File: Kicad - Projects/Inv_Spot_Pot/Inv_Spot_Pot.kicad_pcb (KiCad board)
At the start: 2 copper layers, 190 x 179.5 mm, 107 parts, among them J2 PWM, J3 Display_Power, J4 24V, J5 24V, J6 PWM, K1 Y14x-1C-xxDS, Q1 60N60, Q2 60N60, Q3 60N60, Q4 60N60, U2 LTV-817S

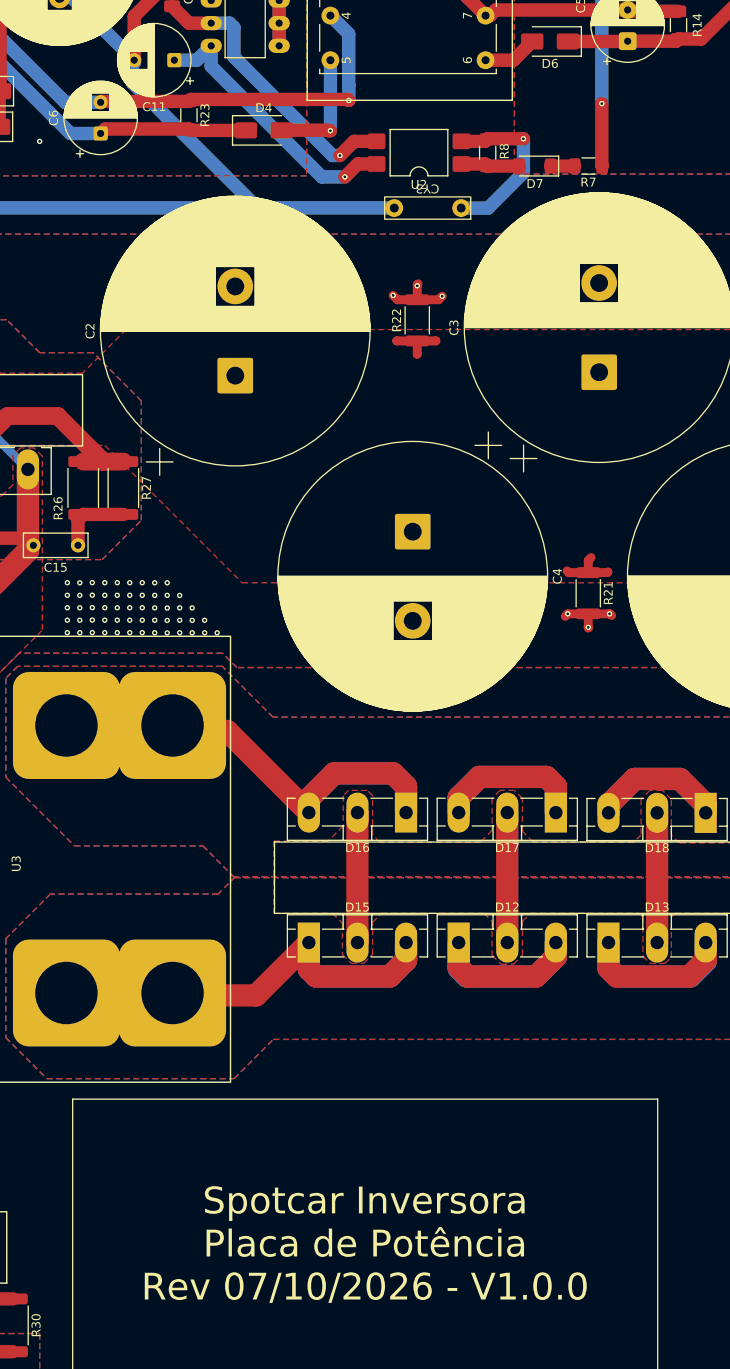
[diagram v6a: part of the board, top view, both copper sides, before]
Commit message: Atualizada Revisão da Placa
Atualizada revisão da placa de potência (07/10/2026, V1.0.0 -> 27/10/2026, V1.1.0)
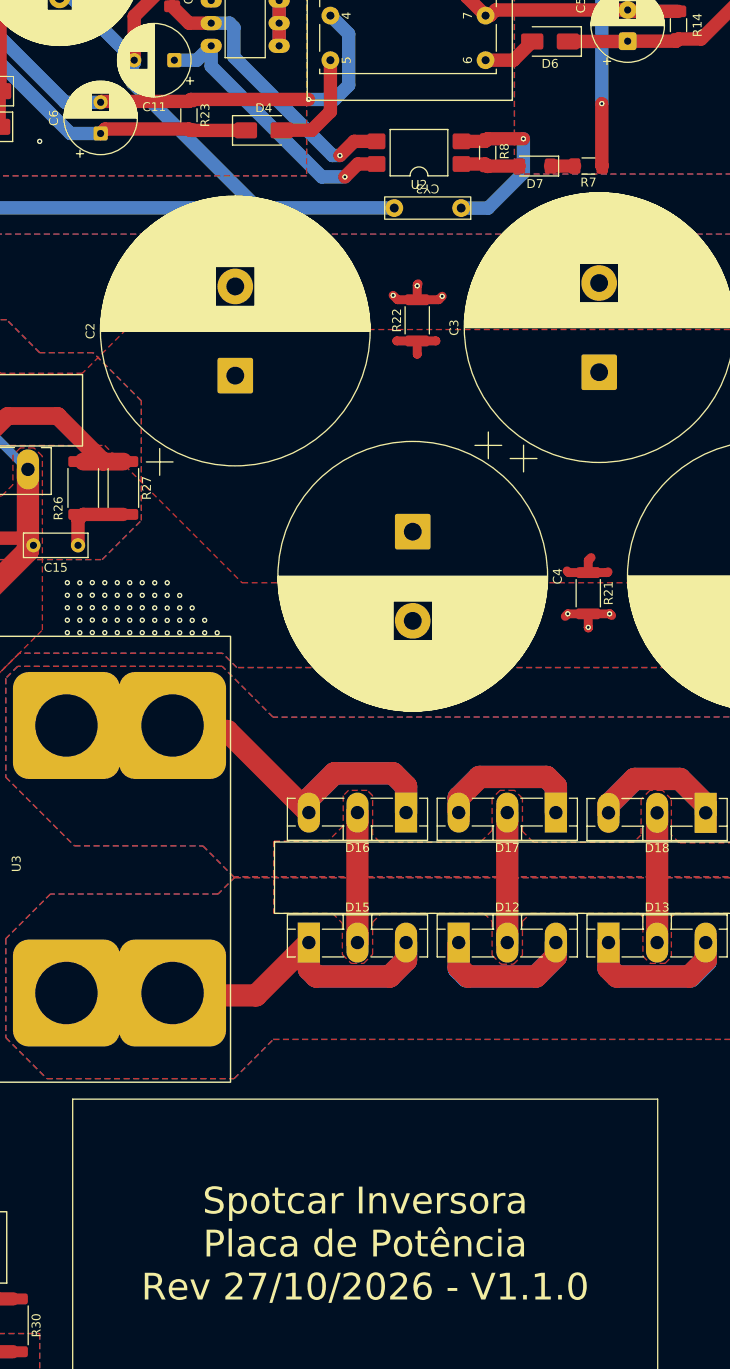
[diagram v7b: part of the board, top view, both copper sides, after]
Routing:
- net Net-(D4-A): track 13.4 -> 12.1 mm, vias 1 -> 0
- net GND_{24}: track 202.5 -> 201.4 mm
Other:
- board text added: "Spotcar Inversora Placa de Potência Rev 27/10/2026 - V1.1.0"
- board text removed: "Spotcar Inversora Placa de Potência Rev 07/10/2026 - V1.0.0"
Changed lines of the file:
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@@
 		(capping no)
 		(filling no)
-		(zone_defaults)
 		(pcbplotparams
 			(layerselection 0x00000000_00000000_55555555_55555571)
@@
 		)
 	)
-	(gr_text "Spotcar Inversora\nPlaca de Potência\nRev 07/10/2026 - V1.0.0"
+	(gr_text "Spotcar Inversora\nPlaca de Potência\nRev 27/10/2026 - V1.1.0"
 		(at 141.9 171.15 0)
 		(layer "F.SilkS")
@@
 	)
 	(segment
-		(start 122.352065 42.8)
-		(end 122.133 43.019065)
-		(width 1.5)
-		(layer "F.Cu")
-		(net "GND_{24}")
-	)
-	(segment
 		(start 17.97 35.3925)
 		(end 17.97 23.68)
@@
 	)
 	(segment
-		(start 139.95 42.8)
-		(end 122.352065 42.8)
-		(width 1.5)
-		(layer "F.Cu")
-		(net "GND_{24}")
-	)
-	(segment
 		(start 22.4525 19.1975)
 		(end 23.83 19.1975)
@@
 	)
 	(segment
+		(start 122.352065 42.8)
+		(end 122.133 43.019065)
+		(width 1.5)
+		(layer "F.Cu")
+		(net "GND_{24}")
+	)
+	(segment
 		(start 82.598 15.909065)
 		(end 81.399497 14.710562)
@@
 	)
 	(segment
+		(start 135.55 42.8)
+		(end 122.352065 42.8)
+		(width 1.5)
+		(layer "F.Cu")
+		(net "GND_{24}")
+	)
+	(segment
 		(start 100.733 15.469065)
 		(end 105.808435 15.469065)
@@
 	)
 	(segment
-		(start 140.06 42.91)
-		(end 139.95 42.8)
-		(width 1.5)
-		(layer "F.Cu")
-		(net "GND_{24}")
-	)
-	(segment
 		(start 81.399497 14.710562)
 		(end 31.879438 14.710562)
@@
 	)
 	(via
-		(at 140.06 42.91)
+		(at 135.55 42.8)
 		(size 0.6)
 		(drill 0.3)
@@
 	)
 	(segment
-		(start 140.06 41.22)
-		(end 140.05 41.21)
+		(start 135.55 42.8)
+		(end 138.46 42.8)
 		(width 1.5)
 		(layer "B.Cu")
@@
 	)
 	(segment
-		(start 140.05 35.45)
-		(end 138 33.4)
+		(start 138.46 42.8)
+		(end 140.05 41.21)
 		(width 1.5)
 		(layer "B.Cu")
@@
 	)
 	(segment
-		(start 140.05 41.21)
-		(end 140.05 35.45)
+		(start 140.05 35.45)
+		(end 138 33.4)
 		(width 1.5)
 		(layer "B.Cu")
@@
 	)
 	(segment
-		(start 140.06 42.91)
-		(end 140.06 41.22)
+		(start 140.05 41.21)
+		(end 140.05 35.45)
 		(width 1.5)
 		(layer "B.Cu")
@@
 	)
 	(segment
-		(start 132.552065 46.25)
-		(end 132.533 46.269065)
+		(start 138 44.17)
+		(end 135.92 46.25)
 		(width 1.5)
 		(layer "F.Cu")
@@
 	)
 	(segment
-		(start 137.72 46.25)
-		(end 132.552065 46.25)
+		(start 132.552065 46.25)
+		(end 132.533 46.269065)
 		(width 1.5)
 		(layer "F.Cu")
@@
 	)
 	(segment
-		(start 138 46.31)
-		(end 137.78 46.31)
+		(start 135.92 46.25)
+		(end 132.552065 46.25)
 		(width 1.5)
 		(layer "F.Cu")
@@
 	)
 	(segment
-		(start 137.78 46.31)
-		(end 137.72 46.25)
+		(start 138 38.4)
+		(end 138 44.17)
 		(width 1.5)
 		(layer "F.Cu")
 		(net "Net-(D4-A)")
 	)
-	(via
-		(at 138 46.31)
-		(size 0.6)
-		(drill 0.3)
-		(layers "F.Cu" "B.Cu")
-		(net "Net-(D4-A)")
-	)
-	(segment
-		(start 138 46.31)
-		(end 138 38.4)
-		(width 1.5)
-		(layer "B.Cu")
-		(net "Net-(D4-A)")
-	)
 	(segment
 		(start 44.033 182.450315)
@@
 	)
 	(segment
+		(start 48.9125 76.76)
+		(end 51.8125 76.76)
+		(width 1.5)
+		(layer "F.Cu")
+		(net "Net-(D8-K)")
+	)
+	(segment
+		(start 51.8125 76.76)
+		(end 52.0025 76.95)
+		(width 1.5)
+		(layer "F.Cu")
+		(net "Net-(D8-K)")
+	)
+	(segment
+		(start 48.521565 73.269065)
+		(end 48.9125 73.66)
+		(width 1.5)
+		(layer "F.Cu")
+		(net "PWM")
+	)
+	(segment
+		(start 51.5825 73.67)
+		(end 48.9225 73.67)
+		(width 1.5)
+		(layer "F.Cu")
+		(net "PWM")
+	)
+	(segment
+		(start 48.9225 73.67)
+		(end 48.9125 73.66)
+		(width 1.5)
+		(layer "F.Cu")
+		(net "PWM")
+	)
+	(segment
+		(start 41.133 73.269065)
+		(end 48.521565 73.269065)
+		(width 1.5)
+		(layer "F.Cu")
+		(net "PWM")
+	)
+	(segment
 		(start 104.083 93.417)
 		(end 104.083 84.284065)
@@
 	)
 	(segment
-		(start 48.521565 73.269065)
-		(end 48.9125 73.66)
-		(width 1.5)
-		(layer "F.Cu")
-		(net "PWM")
-	)
-	(segment
-		(start 51.5825 73.67)
-		(end 48.9225 73.67)
-		(width 1.5)
-		(layer "F.Cu")
-		(net "PWM")
-	)
-	(segment
-		(start 48.9225 73.67)
-		(end 48.9125 73.66)
-		(width 1.5)
-		(layer "F.Cu")
-		(net "PWM")
-	)
-	(segment
-		(start 41.133 73.269065)
-		(end 48.521565 73.269065)
-		(width 1.5)
-		(layer "F.Cu")
-		(net "PWM")
-	)
-	(segment
 		(start 184.5625 24.3)
 		(end 184.5625 19.499565)
@@
 	)
 	(segment
+		(start 93.24 84.341065)
+		(end 93.183 84.284065)
+		(width 1.5)
+		(layer "F.Cu")
+		(net "Gate")
+	)
+	(segment
+		(start 58.62 76.95)
+		(end 56.0025 76.95)
+		(width 1.5)
+		(layer "F.Cu")
+		(net "Gate")
+	)
+	(segment
+		(start 93.24 88.8675)
+		(end 93.24 84.341065)
+		(width 1.5)
+		(layer "F.Cu")
+		(net "Gate")
+	)
+	(segment
+		(start 56.0025 76.95)
+		(end 56.0025 74.99)
+		(width 1.5)
+		(layer "F.Cu")
+		(net "Gate")
+	)
+	(segment
+		(start 56.0025 74.99)
+		(end 54.6825 73.67)
+		(width 1.5)
+		(layer "F.Cu")
+		(net "Gate")
+	)
+	(via
+		(at 58.62 76.95)
+		(size 0.6)
+		(drill 0.3)
+		(layers "F.Cu" "B.Cu")
+		(net "Gate")
+	)
+	(segment
+		(start 59.34 76.95)
+		(end 60.424065 78.034065)
+		(width 1)
+		(layer "B.Cu")
+		(net "Gate")
+	)
+	(segment
+		(start 86.933 78.034065)
+		(end 93.183 84.284065)
+		(width 1)
+		(layer "B.Cu")
+		(net "Gate")
+	)
+	(segment
+		(start 58.62 76.95)
+		(end 59.34 76.95)
+		(width 1)
+		(layer "B.Cu")
+		(net "Gate")
+	)
+	(segment
+		(start 60.424065 78.034065)
+		(end 86.933 78.034065)
+		(width 1)
+		(layer "B.Cu")
+		(net "Gate")
+	)
+	(segment
 		(start 42.51 25.16)
 		(end 42.5 25.17)
@@
 		(net "/PWM_L")
 	)
-	(segment
-		(start 93.24 84.341065)
-		(end 93.183 84.284065)
-		(width 1.5)
-		(layer "F.Cu")
-		(net "Gate")
-	)
-	(segment
-		(start 58.62 76.95)
-		(end 56.0025 76.95)
-		(width 1.5)
-		(layer "F.Cu")
-		(net "Gate")
-	)
-	(segment
-		(start 93.24 88.8675)
-		(end 93.24 84.341065)
-		(width 1.5)
-		(layer "F.Cu")
-		(net "Gate")
-	)
-	(segment
-		(start 56.0025 76.95)
-		(end 56.0025 74.99)
-		(width 1.5)
-		(layer "F.Cu")
-		(net "Gate")
-	)
-	(segment
-		(start 56.0025 74.99)
-		(end 54.6825 73.67)
-		(width 1.5)
-		(layer "F.Cu")
-		(net "Gate")
-	)
-	(via
-		(at 58.62 76.95)
-		(size 0.6)
-		(drill 0.3)
-		(layers "F.Cu" "B.Cu")
-		(net "Gate")
-	)
-	(segment
-		(start 59.34 76.95)
-		(end 60.424065 78.034065)
-		(width 1)
-		(layer "B.Cu")
-		(net "Gate")
-	)
-	(segment
-		(start 86.933 78.034065)
-		(end 93.183 84.284065)
-		(width 1)
-		(layer "B.Cu")
-		(net "Gate")
-	)
-	(segment
-		(start 58.62 76.95)
-		(end 59.34 76.95)
-		(width 1)
-		(layer "B.Cu")
-		(net "Gate")
-	)
-	(segment
-		(start 60.424065 78.034065)
-		(end 86.933 78.034065)
-		(width 1)
-		(layer "B.Cu")
-		(net "Gate")
-	)
-	(segment
-		(start 48.9125 76.76)
-		(end 51.8125 76.76)
-		(width 1.5)
-		(layer "F.Cu")
-		(net "Net-(D8-K)")
-	)
-	(segment
-		(start 51.8125 76.76)
-		(end 52.0025 76.95)
-		(width 1.5)
-		(layer "F.Cu")
-		(net "Net-(D8-K)")
-	)
 	(zone

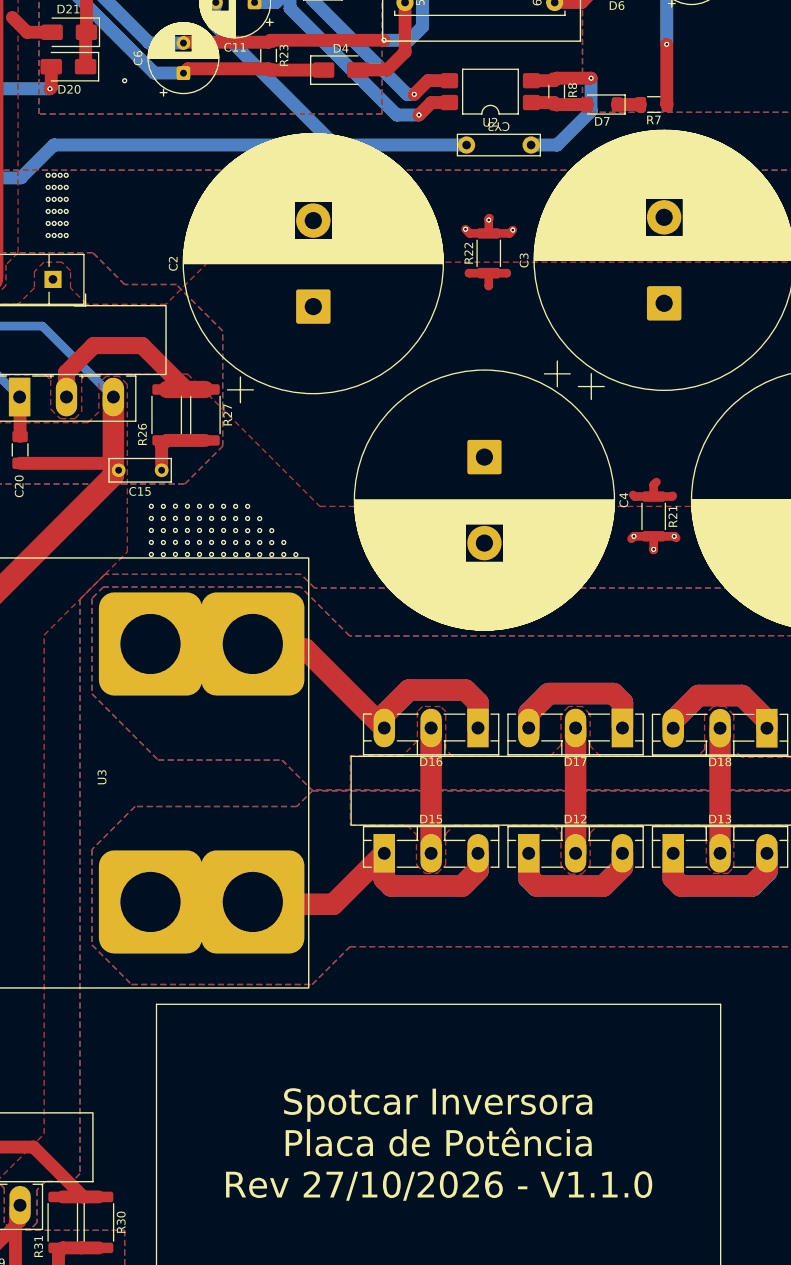
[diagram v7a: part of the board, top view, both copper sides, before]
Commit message: Adicionada Proteção
Adicionado código da proteção térmica

Adicionado limite de tempo na ponteira de aquecimento
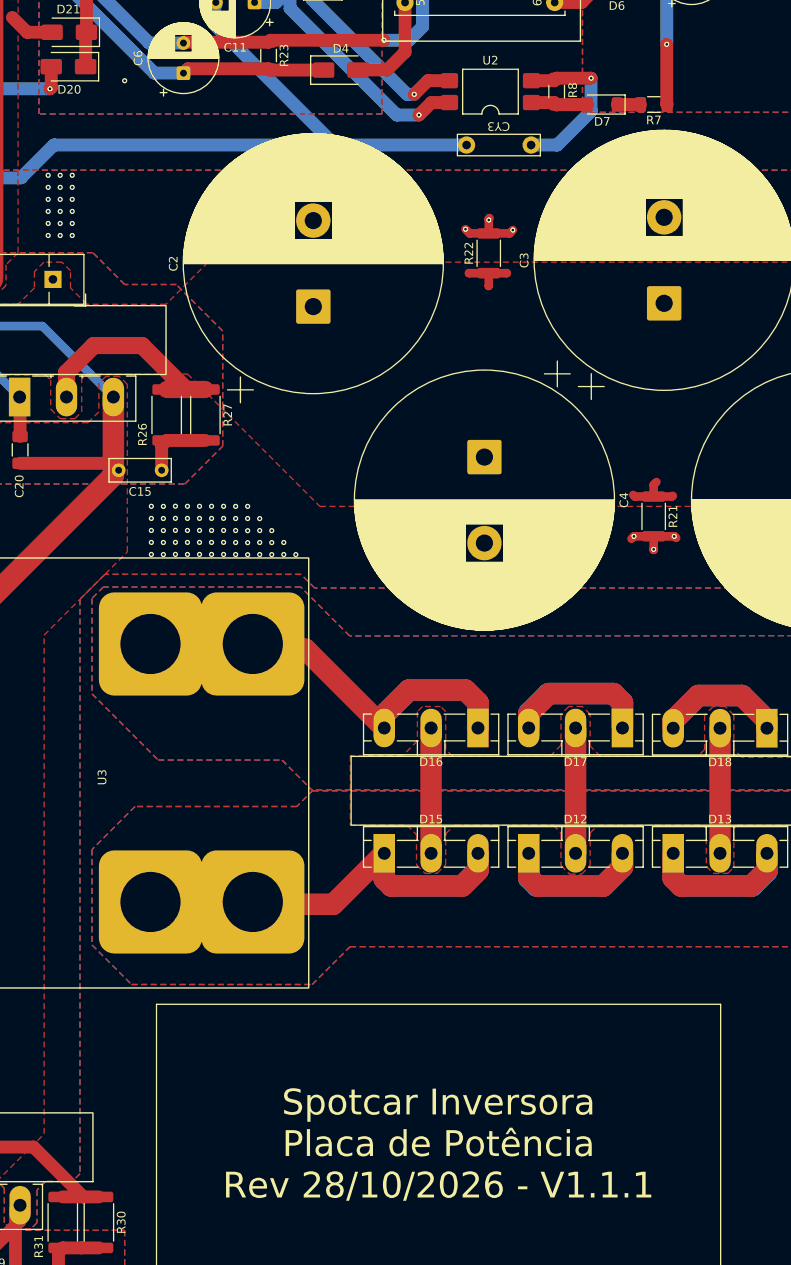
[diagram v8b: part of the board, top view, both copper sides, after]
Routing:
- net Earth: vias 104 -> 98
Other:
- board text added: "Spotcar Inversora Placa de Potência Rev 28/10/2026 - V1.1.1"
- board text removed: "Spotcar Inversora Placa de Potência Rev 27/10/2026 - V1.1.0"
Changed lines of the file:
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@@
 		(tags "SMD DIP DIL PDIP SMDIP 2.54mm 9.53mm 375mil")
 		(property "Reference" "U2"
-			(at 0 -3.6 0)
+			(at 0 3.619065 0)
 			(layer "F.SilkS")
 			(effects
@@
 	(gr_poly
 		(pts
-			(xy 60.2 176.3) (xy 65.8 170.7) (xy 65.8 155.1) (xy 48.8 155.1) (xy 48.8 170.6) (xy 54.5 176.3)
+			(xy 59.428209 175.526899) (xy 65.67 169.28) (xy 65.67 167.5) (xy 48.8 167.5) (xy 48.8 169.85) (xy 54.472347 175.525515)
 		)
 		(stroke
@@
 	(gr_poly
 		(pts
-			(xy 90.5 175.5) (xy 96.1 169.9) (xy 96.1 154.3) (xy 79.1 154.3) (xy 79.1 169.8) (xy 84.8 175.5)
+			(xy 90.5 175.5) (xy 96.03 169.97) (xy 96.03 167.64) (xy 79.1 167.64) (xy 79.1 169.8) (xy 84.8 175.5)
 		)
 		(stroke
@@
 		)
 	)
-	(gr_text "Spotcar Inversora\nPlaca de Potência\nRev 27/10/2026 - V1.1.0"
+	(gr_text "Spotcar Inversora\nPlaca de Potência\nRev 28/10/2026 - V1.1.1"
 		(at 141.9 171.15 0)
 		(layer "F.SilkS")
@@
 	)
 	(via
-		(at 111.3 98.39)
+		(at 99.3 58.5)
 		(size 0.6)
 		(drill 0.3)
@@
 	)
 	(via
-		(at 119.7 99.83)
+		(at 111.3 98.39)
 		(size 0.6)
 		(drill 0.3)
@@
 	)
 	(via
-		(at 96.5 58.5)
+		(at 119.7 99.83)
 		(size 0.6)
 		(drill 0.3)
@@
 	)
 	(via
-		(at 34.4 169.2)
+		(at 96.5 58.5)
 		(size 0.6)
 		(drill 0.3)
@@
 	)
 	(via
-		(at 109.9 97)
+		(at 34.4 169.2)
 		(size 0.6)
 		(drill 0.3)
@@
 	)
 	(via
-		(at 118.3 102.6)
+		(at 109.9 97)
 		(size 0.6)
 		(drill 0.3)
@@
 	)
 	(via
-		(at 112.7 99.8)
+		(at 118.3 102.6)
 		(size 0.6)
 		(drill 0.3)
@@
 	)
 	(via
-		(at 97.2 62.7)
+		(at 112.7 99.8)
 		(size 0.6)
 		(drill 0.3)
@@
 	)
 	(via
-		(at 98.6 61.3)
-		(size 0.6)
-		(drill 0.3)
-		(layers "F.Cu" "B.Cu")
-		(free yes)
-		(net "Earth")
-	)
-	(via
 		(at 116.9 96.99)
 		(size 0.6)
@@
 	)
 	(via
-		(at 97.2 64.1)
-		(size 0.6)
-		(drill 0.3)
-		(layers "F.Cu" "B.Cu")
-		(free yes)
-		(net "Earth")
-	)
-	(via
 		(at 112.7 98.4)
 		(size 0.6)
@@
 	)
 	(via
-		(at 97.2 61.3)
-		(size 0.6)
-		(drill 0.3)
-		(layers "F.Cu" "B.Cu")
-		(free yes)
-		(net "Earth")
-	)
-	(via
 		(at 119.7 101.22)
 		(size 0.6)
@@
 	)
 	(via
-		(at 98.6 59.9)
-		(size 0.6)
-		(drill 0.3)
-		(layers "F.Cu" "B.Cu")
-		(free yes)
-		(net "Earth")
-	)
-	(via
-		(at 97.2 65.5)
-		(size 0.6)
-		(drill 0.3)
-		(layers "F.Cu" "B.Cu")
-		(free yes)
-		(net "Earth")
-	)
-	(via
 		(at 115.5 98.4)
 		(size 0.6)
@@
 	)
 	(via
-		(at 98.6 64.1)
-		(size 0.6)
-		(drill 0.3)
-		(layers "F.Cu" "B.Cu")
-		(free yes)
-		(net "Earth")
-	)
-	(via
-		(at 97.2 59.9)
-		(size 0.6)
-		(drill 0.3)
-		(layers "F.Cu" "B.Cu")
-		(free yes)
-		(net "Earth")
-	)
-	(via
 		(at 34.4 169.9)
 		(size 0.6)
@@
 	)
 	(via
+		(at 99.3 64.1)
+		(size 0.6)
+		(drill 0.3)
+		(layers "F.Cu" "B.Cu")
+		(free yes)
+		(net "Earth")
+	)
+	(via
 		(at 114.1 96.99)
 		(size 0.6)
@@
 	)
 	(via
-		(at 109.9 102.6)
+		(at 99.3 62.7)
 		(size 0.6)
 		(drill 0.3)
@@
 	)
 	(via
-		(at 35.9 98.8)
+		(at 109.9 102.6)
 		(size 0.6)
 		(drill 0.3)
@@
 	)
 	(via
-		(at 115.5 96.99)
+		(at 35.9 98.8)
 		(size 0.6)
 		(drill 0.3)
@@
 	)
 	(via
-		(at 98.6 65.5)
+		(at 115.5 96.99)
 		(size 0.6)
 		(drill 0.3)
@@
 	)
 	(via
-		(at 98.6 58.5)
+		(at 35.2 97.4)
 		(size 0.6)
 		(drill 0.3)
@@
 	)
 	(via
-		(at 35.2 97.4)
+		(at 119.7 102.62)
 		(size 0.6)
 		(drill 0.3)
@@
 	)
 	(via
-		(at 119.7 102.62)
+		(at 109.9 99.81)
 		(size 0.6)
 		(drill 0.3)
@@
 	)
 	(via
-		(at 97.2 58.5)
+		(at 197.4 81.6)
 		(size 0.6)
 		(drill 0.3)
@@
 	)
 	(via
-		(at 109.9 99.81)
+		(at 169.3 100.481565)
 		(size 0.6)
 		(drill 0.3)
 		(layers "F.Cu" "B.Cu")
-		(free yes)
 		(net "Earth")
 	)
 	(via
-		(at 197.4 81.6)
+		(at 115.5 101.19)
 		(size 0.6)
 		(drill 0.3)
@@
 	)
 	(via
-		(at 169.3 100.481565)
+		(at 99.3 61.3)
 		(size 0.6)
 		(drill 0.3)
 		(layers "F.Cu" "B.Cu")
+		(free yes)
 		(net "Earth")
 	)
 	(via
-		(at 115.5 101.19)
+		(at 35.1 169.9)
 		(size 0.6)
 		(drill 0.3)
@@
 	)
 	(via
-		(at 35.1 169.9)
+		(at 97.9 59.9)
 		(size 0.6)
 		(drill 0.3)
@@
 	)
 	(via
-		(at 97.9 59.9)
+		(at 112.7 102.59)
 		(size 0.6)
 		(drill 0.3)
@@
 	)
 	(via
-		(at 112.7 102.59)
+		(at 99.3 65.5)
 		(size 0.6)
 		(drill 0.3)
@@
 	)
 	(via
-		(at 35.9 99.5)
+		(at 99.3 59.9)
 		(size 0.6)
 		(drill 0.3)
@@
 	)
 	(via
-		(at 98.6 62.7)
+		(at 35.9 99.5)
 		(size 0.6)
 		(drill 0.3)
@@
 			)
 		)
+	)
+	(zone
+		(layer "F.Cu")
+		(hatch edge 0.5)
+		(connect_pads
+			(clearance 0)
+		)
+		(min_thickness 0.25)
+		(keepout
+			(tracks allowed)
+			(vias allowed)
+			(pads allowed)
+			(copperpour not_allowed)
+			(footprints allowed)
+		)
+		(placement
+			(enabled no)
+			(sheetname "/")
+		)
+		(fill
+			(thermal_gap 0.5)
+			(thermal_bridge_width 0.5)
+			(island_removal_mode 0)
+		)
+		(polygon
+			(pts
+				(xy 45.05 180.769065) (xy 62.36 180.769065) (xy 62.36 191.53) (xy 45.05 191.53)
+			)
+		)
